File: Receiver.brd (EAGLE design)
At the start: 71.1 x 62.2 mm, 11 parts, among them IC1 25LC080P, J1 PIC_ICSP_6_PIN, U1 915MHz, U2 DS3234, X1 BU-SMA-V

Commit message: Updates
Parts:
- added BUTTON: TSW-106-02-S-S, con-samtec:TSW-106-02-S-S
- added C3, C4: (no value), resistor:C050-025X075
- added PWR: 22-27-2021-02, con-molex:6410-02
- added SJ1: SOLDERJUMPERNO, SparkFun-Retired:SJ_2S-NO
- moved RA8875 33.2 mm to (5.08, 41.9)
- moved X1 26.1 mm to (40.6, 5.08)
- moved IC1 18.2 mm to (20.3, 19.1), flipped to the bottom, turned to 270 degrees
- moved U1 13.3 mm to (40.6, 17.8)
- moved U2 13.3 mm to (40.6, 17.8)
- moved BT1 12.5 mm to (40.6, 43.2)
- moved Q1 2.54 mm to (5.08, 19.1)
- moved C1 2.29 mm to (1.91, 15.2), turned to 90 degrees
- moved C2 2.29 mm to (1.91, 22.9), turned to 270 degrees
- moved J1 1.27 mm to (14.0, 59.7)
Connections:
- net N$10 renamed MOSI1
- net N$11 renamed MOSI2
- net N$6 renamed SCK1
- net N$7 renamed MISO1
- net N$8 renamed SCK2
- net N$9 renamed MISO2
- new net N$10: BUTTON.4, U$1.19
- new net N$11: BUTTON.6, U$1.22
- new net N$17: RA8875.8, U$1.6
- new net N$18: RA8875.4, U$1.2
- new net N$19: RA8875.10, U$1.9
- new net N$20: RA8875.11, U$1.10
- new net N$21: U$1.30, U1.14
- new net N$22: J1.5, SJ1.1
- new net N$6: BUTTON.1, U$1.15
- new net N$7: BUTTON.2, U$1.16
- new net N$8: BUTTON.3, U$1.17
- new net N$9: BUTTON.5, U$1.20
- net +3V3: now also C3.1, C4.1, PWR.1, RA8875.1, SJ1.2; no longer J1.5
- net GND: now also C3.2, C4.2, PWR.2
- net N$12: now also U$1.29; no longer U$1.22
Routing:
- net +3V3: track 85.8 -> 141.4 mm, vias 1 -> 3
- net MISO1: track 0.00 -> 53.4 mm, vias 0 -> 1
- net SCK1: track 0.00 -> 48.0 mm
- net N$21: track 0.00 -> 31.8 mm, vias 0 -> 1
- net MISO2: track 75.8 -> 48.7 mm, vias 0 -> 1
- net MOSI1: track 0.00 -> 23.4 mm
- net N$11: track 0.00 -> 20.3 mm
- net GND: track 17.3 -> 0.00 mm
- net N$16: track 24.7 -> 14.3 mm
- net N$15: track 19.1 -> 10.2 mm, vias 1 -> 0
- net N$17: track 0.00 -> 8.15 mm
- net N$20: track 0.00 -> 8.15 mm
- net N$19: track 0.00 -> 8.15 mm
- net N$18: track 0.00 -> 8.15 mm
- net N$14: track 65.7 -> 58.2 mm
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- added copper zone on layer 1, net GND
- added copper zone on layer 16, net GND
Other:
- board size 71.1 x 62.2 mm -> 53.3 x 63.5 mm

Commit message: Ordered sender PCB
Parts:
- added IC2: 25LC080P, microchip:DIL8
- added J2: (no value), SparkFun-Connectors:1X01
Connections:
- net +3V3: now also IC1.3, IC1.7, IC2.3, IC2.7, IC2.8
- net GND: now also IC2.4, J2.1
- net MISO2: now also IC2.2
- net MOSI2: now also IC2.5
- net SCK2: now also IC2.6
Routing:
- net +3V3: track 141.4 -> 175.7 mm
- net MOSI2: track 33.3 -> 47.8 mm
- net MISO2: track 48.7 -> 62.1 mm
- net SCK2: track 54.1 -> 67.4 mm, vias 3 -> 5
- net MISO1: track 53.4 -> 54.9 mm

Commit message: Updated receiver PCB
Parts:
- removed J1: PIC_ICSP_6_PIN, SparkFun-Connectors:MOLEX-1X6
- added IC3: (no value), v-reg:78XXS
- added PWR1: 22-27-2021-02, con-molex:6410-02
- added R1, R2, R3, R4, R5, R6: (no value), resistor:M1206
- added X2: 53047-05, con-molex:53047-05
- moved J2 5.12 mm to (1.91, 6.99)
- moved C1 1.42 mm to (1.27, 16.5), turned to 270 degrees
- moved C2 1.42 mm to (1.27, 21.6), turned to 90 degrees
- moved BUTTON 0.63 mm to (10.2, 8.26)
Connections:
- new net N$23: IC2.1, U$1.25
- new net N$24: IC3.IN, PWR1.1
- net +3V3: now also IC3.OUT, R1.2, R2.2, R3.2, R4.2, R5.2, R6.2
- net GND: now also IC3.GND, PWR1.2, X2.3; no longer J1.4
- net N$1: now also X2.4; no longer J1.3
- net N$10: now also R4.1
- net N$11: now also R6.1
- net N$2: now also X2.5; no longer J1.2
- net N$22: now also X2.2; no longer J1.5
- net N$3: now also X2.1; no longer J1.6
- net N$6: now also R1.1
- net N$7: now also R2.1
- net N$8: now also R3.1
- net N$9: now also R5.1
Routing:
- net +3V3: track 175.7 -> 207.5 mm
- net N$24: track 0.00 -> 10.5 mm
- net N$3: track 20.6 -> 11.2 mm, vias 0 -> 1
- net N$23: track 0.00 -> 4.34 mm
- net N$2: track 20.6 -> 17.3 mm
- net N$22: track 3.99 -> 6.51 mm
- net N$11: track 20.3 -> 22.4 mm
- net N$9: track 3.96 -> 5.74 mm
- net N$8: track 3.44 -> 5.21 mm
- net N$7: track 3.44 -> 5.21 mm
- net N$6: track 3.44 -> 5.21 mm
- net N$10: track 3.96 -> 5.74 mm
- net N$1: track 15.5 -> 14.2 mm

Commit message: Receiver board r2
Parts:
- removed BT1: (no value), SparkFun-Batteries:BATTCON_20MM
- removed BUTTON: TSW-106-02-S-S, con-samtec:TSW-106-02-S-S
- removed IC1, IC2: 25LC080P, microchip:DIL8
- removed IC3: (no value), v-reg:78XXS
- removed PWR1: 22-27-2021-02, con-molex:6410-02
- removed Q1: (no value), crystal:HC49U-V
- removed R2, R3, R4, R5, R6: (no value), resistor:M1206
- removed SJ1: SOLDERJUMPERNO, SparkFun-Retired:SJ_2S-NO
- removed U$1: PIC18F47K40, microchip:DIL40
- added C5, C6: (no value), resistor:C1206
- added C7: 0.1uF, resistor:C1206
- added I2C-DBG: (no value), SparkFun-Connectors:1X03
- added J1: SD_CARD_SOCKET, SparkFun-Connectors:SD
- added RA8875-DBG: (no value), SparkFun-Connectors:1X09
- added SPI2-DBG: (no value), SparkFun-Connectors:1X08
- added TP3V3, TPCLKOUT, TPSQW, TPVBUS: TPB2,54, testpad:B2,54
- added U$3: (no value), adafruit:CR1220-SMD
- added U4: FT232RL, SparkFun-IC-Comms:SSOP28DB
- added U5: DS1374C, FRC696:SO-16DW
- added U6: +12v, SparkFun-IC-Power:TO-252
- added UARTDBG: 53047-03, con-molex:53047-03
- C1: value (none) -> 0.1uF
- C2: value (none) -> 1uF
- C3: value (none) -> 0.1uF; device resistor:C050-025X075 -> resistor:C1206
- C4: value (none) -> 1uF; device resistor:C050-025X075 -> resistor:C1206
- J2: device SparkFun-Connectors:1X01 -> SparkFun-Connectors:USB-B-MICRO-SMD
- PWR: value 22-27-2021-02 -> 53261-02; device con-molex:6410-02 -> con-molex:53261-02
- R1: value (none) -> 10k; device resistor:M1206 -> resistor:R1206
- RA8875: value C-GRID-11-70543 -> C-GRID-10-70543; device con-molex:70543-11 -> con-molex:70543-10
- U1: value 915MHz -> PIC18F47Q84; device SparkFun-RF:RFM69HCW-XXXS2 -> FRC696:DIL40
- U2: value DS3234 -> 915MHz; device SparkFun-Clocks:SO20-0.3 -> SparkFun-RF:RFM69HCW-XXXS2
- X2: value 53047-05 -> PIC-PROG047; device con-molex:53047-05 -> FRC696:53047-05
- moved J2 88.5 mm to (73.0, 59.7), turned to 180 degrees
- moved C1 82.2 mm to (59.1, 74.9), flipped to the top
- moved C2 75.9 mm to (55.2, 74.9), flipped to the top, turned to 270 degrees
- moved R1 60.3 mm to (18.4, 73.7), flipped to the top, turned to 90 degrees
- moved X1 47.7 mm to (63.5, 47.0)
- moved PWR 41.3 mm to (71.8, 69.8), turned to 270 degrees
- moved RA8875 36.3 mm to (24.8, 11.4), turned to 0 degrees
- moved U1 30.4 mm to (26.0, 44.5), turned to 270 degrees
- moved X2 20.8 mm to (26.0, 73.7)
- moved C3 19.9 mm to (40.0, 73.7), turned to 270 degrees
- moved U2 17.6 mm to (56.5, 25.4), flipped to the top
- moved C4 13.1 mm to (36.2, 73.7), turned to 270 degrees
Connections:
- removed net N$14: BT1.1, U2.16
- removed net N$15: U$1.24, U1.5
- removed net N$16: U$1.21, U2.1
- removed net N$17: RA8875.8, U$1.6
- removed net N$18: RA8875.4, U$1.2
- removed net N$19: RA8875.10, U$1.9
- removed net N$20: RA8875.11, U$1.10
- removed net N$21: U$1.30, U1.14
- removed net N$22: SJ1.1, X2.2
- removed net N$23: IC2.1, U$1.25
- removed net N$24: IC3.IN, PWR1.1
- new net CLK_RST: U5.14
- new net RA8875-CS: RA8875-DBG.6, RA8875.7, U1.30
- new net RA8875-INT: RA8875-DBG.9, RA8875.10, U1.23
- new net RA8875-LITE: RA8875-DBG.2, RA8875.3, U1.19
- new net RA8875-RST: RA8875-DBG.7, RA8875.8, U1.29
- new net RA8875-WAIT: RA8875-DBG.8, RA8875.9, U1.28
- new net RF-CS: SPI2-DBG.5, U1.24, U2.5
- new net RF-DIO0: SPI2-DBG.7, U1.26, U2.14
- new net RF-RST: SPI2-DBG.6, U1.25, U2.6
- new net SCL: I2C-DBG.2, U1.38, U5.1
- new net SD-CS: J1.1, SPI2-DBG.8, U1.27
- new net SDA: I2C-DBG.3, U1.37, U5.16
- new net UARTRX: U1.35, U4.1, UARTDBG.3
- new net UARTTX: U1.34, U4.5, UARTDBG.2
- net +3V3: now also C5.1, C6.1, J1.4, TP3V3.TP, U1.11, U1.32, U2.13, U4.20, U4.4, U5.4, U6.2, X2.2; no longer IC1.3, IC1.7, IC1.8, IC2.3, IC2.7, IC2.8, IC3.OUT, PWR.1, R2.2, R3.2, R4.2, R5.2, R6.2, SJ1.2, U$1.11, U$1.32, U1.13, U2.4
- net GND: now also C1.2, C2.2, C5.2, C6.2, C7.2, I2C-DBG.1, J1.3, J1.6, J1.SH@1, J1.SH@2, J2.GND, RA8875-DBG.1, SPI2-DBG.1, U$3.-, U1.12, U1.31, U2.1, U4.18, U4.21, U4.25, U4.26, U4.7, U5.15, U6.3, UARTDBG.1; no longer BT1.2, C1.1, C2.1, IC1.4, IC2.4, IC3.GND, J2.1, PWR1.2, U$1.12, U$1.31, U1.1, U1.10, U1.8, U2.11, U2.12, U2.13, U2.14, U2.15, U2.2, U2.7, U2.9
- net MISO1: now also RA8875-DBG.4, RA8875.5, U1.17; no longer RA8875.6, U$1.23
- net MISO2: now also J1.7, SPI2-DBG.2, U1.21, U2.2; no longer IC1.2, IC2.2, U$1.35, U1.2, U2.19
- net MOSI1: now also RA8875-DBG.5, RA8875.6, U1.16; no longer RA8875.7, U$1.36
- net MOSI2: now also J1.2, SPI2-DBG.3, U1.22, U2.3; no longer IC1.5, IC2.5, U$1.27, U1.3, U2.17
- net N$1: now also U1.39, X2.5; no longer U$1.40, X2.4
- net N$10: now also U$3.+$1, U$3.+$2, U5.13; no longer BUTTON.4, R4.1, U$1.19
- net N$11: now also TPSQW.TP, U5.3; no longer BUTTON.6, R6.1, U$1.22
- net N$12: now also TPCLKOUT.TP, U1.14; no longer IC1.1, U$1.29
- net N$13: now also U2.9; no longer U1.9
- net N$2: now also U1.40, X2.4; no longer U$1.39, X2.5
- net N$3: now also R1.1, U1.1; no longer U$1.1
- net N$4: now also C1.1, C2.1, PWR.1, U6.1; no longer C1.2, Q1.2, U$1.14
- net N$5: now also J2.VBUS, TPVBUS.TP; no longer C2.2, Q1.1, U$1.13
- net N$6: now also C7.1, U4.17; no longer BUTTON.1, R1.1, U$1.15
- net N$7: now also J2.D-, U4.16; no longer BUTTON.2, R2.1, U$1.16
- net N$8: now also J2.D+, U4.15; no longer BUTTON.3, R3.1, U$1.17
- net N$9: now also U1.15; no longer BUTTON.5, R5.1, U$1.20
- net SCK1: now also RA8875-DBG.3, RA8875.4, U1.18; no longer RA8875.5, U$1.18
- net SCK2: now also J1.5, SPI2-DBG.4, U1.20, U2.4; no longer IC1.6, IC2.6, U$1.34, U1.4, U2.18, U2.20
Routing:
- net N$14: track 58.2 -> 0.00 mm, vias 1 -> 0
- net RA8875-CS: track 0.00 -> 45.3 mm
- net RA8875-RST: track 0.00 -> 42.7 mm
- net RA8875-WAIT: track 0.00 -> 40.2 mm
- net SD-CS: track 0.00 -> 39.6 mm
- net SCL: track 0.00 -> 37.3 mm
- net N$10: track 5.74 -> 42.3 mm
- net RF-RST: track 0.00 -> 34.5 mm
- net +3V3: track 207.5 -> 240.9 mm, vias 3 -> 2
- net N$21: track 31.8 -> 0.00 mm, vias 1 -> 0
- net RF-CS: track 0.00 -> 31.1 mm
- net UARTRX: track 0.00 -> 28.5 mm
- net SDA: track 0.00 -> 27.6 mm
- net RA8875-INT: track 0.00 -> 26.8 mm
- net UARTTX: track 0.00 -> 26.1 mm
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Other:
- board size 53.3 x 63.5 mm -> 74.9 x 81.3 mm
- board text added: "TEMP MONITOR R2"

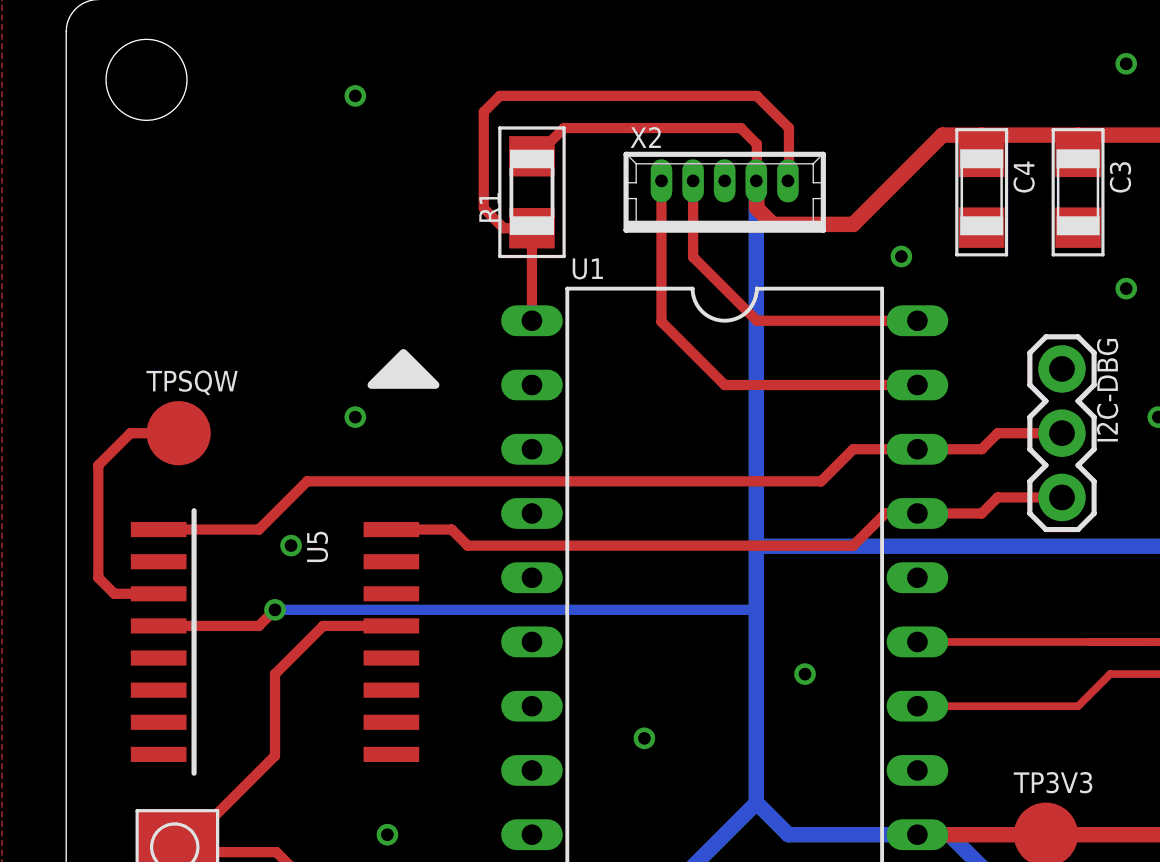
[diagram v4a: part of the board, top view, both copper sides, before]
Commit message: Adding button inputs
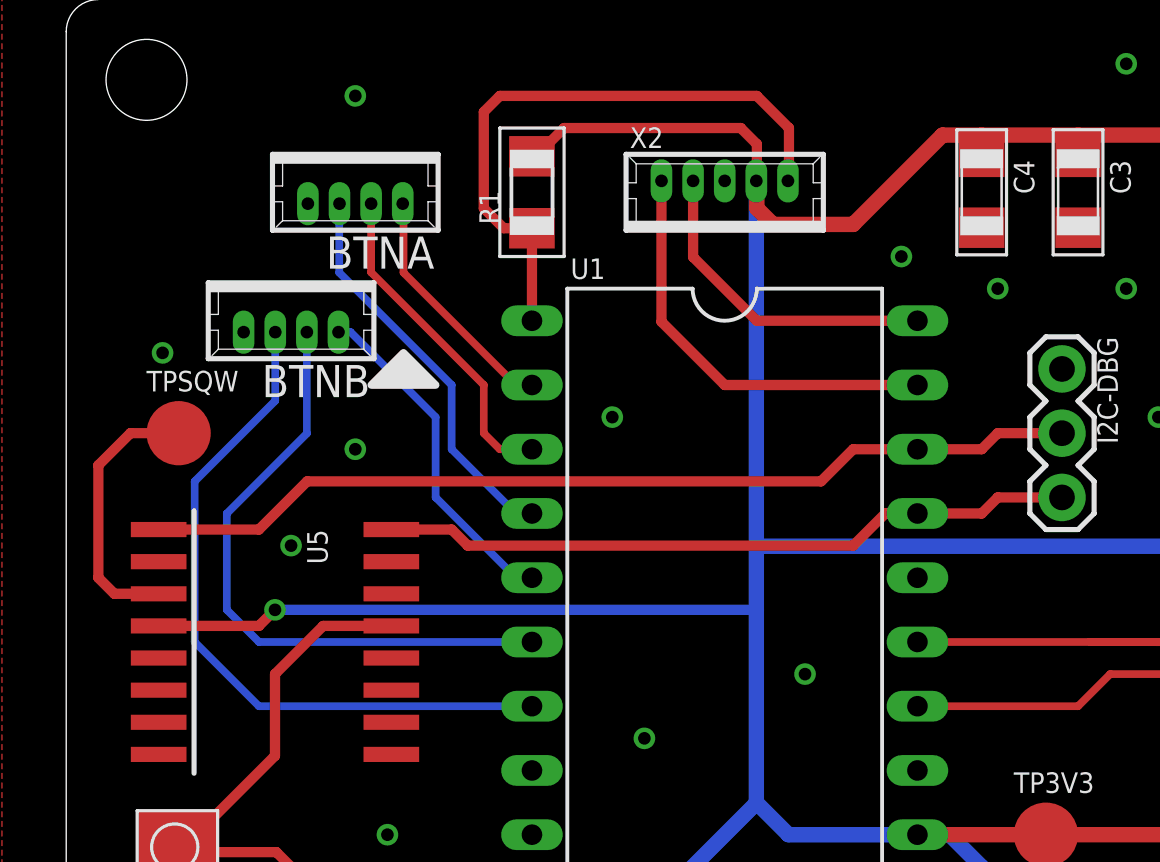
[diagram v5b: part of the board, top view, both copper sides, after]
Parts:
- added BTNA, BTNB: 53047-04, con-molex:53047-04
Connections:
- new net BTN1: BTNA.2, U1.4
- new net BTN2: BTNA.3, U1.3
- new net BTN3: BTNA.4, U1.2
- new net BTN4: BTNB.2, U1.7
- new net BTN5: BTNB.3, U1.6
- new net BTN6: BTNB.4, U1.5
- net GND: now also BTNA.1, BTNB.1
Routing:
- net BTN4: track 0.00 -> 28.0 mm
- net BTN5: track 0.00 -> 24.9 mm
- net BTN1: track 0.00 -> 15.8 mm
- net BTN6: track 0.00 -> 13.5 mm
- net BTN2: track 0.00 -> 13.1 mm
- net BTN3: track 0.00 -> 9.66 mm
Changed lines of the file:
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@@
 <attribute name="VALUE" x="37.338" y="67.945" size="0.6096" layer="27" font="vector" ratio="20" rot="R270"/>
+</element>
+<element name="BTNB" library="con-molex" package="53047-04" value="53047-04" x="8.89" y="68.58" smashed="yes" rot="R180">
+<attribute name="MF" value="WALDOM/MOLEX" x="8.89" y="68.58" size="0.8128" layer="27" font="fixed" rot="R180" display="off"/>
+<attribute name="OC_NEWARK" value="38C9900" x="8.89" y="68.58" size="0.8128" layer="27" font="fixed" rot="R180" display="off"/>
+<attribute name="OC_FARNELL" value="9733060" x="8.89" y="68.58" size="0.8128" layer="27" font="fixed" rot="R180" display="off"/>
+<attribute name="MPN" value="53047-0410" x="8.89" y="68.58" size="0.8128" layer="27" font="fixed" rot="R180" display="off"/>
+<attribute name="NAME" x="12.015" y="66.83" size="1.27" layer="25" font="fixed" rot="R180"/>
+</element>
+<element name="BTNA" library="con-molex" package="53047-04" value="53047-04" x="11.43" y="73.66" smashed="yes" rot="R180">
+<attribute name="MF" value="WALDOM/MOLEX" x="11.43" y="73.66" size="0.8128" layer="27" font="fixed" rot="R180" display="off"/>
+<attribute name="OC_NEWARK" value="38C9900" x="11.43" y="73.66" size="0.8128" layer="27" font="fixed" rot="R180" display="off"/>
+<attribute name="OC_FARNELL" value="9733060" x="11.43" y="73.66" size="0.8128" layer="27" font="fixed" rot="R180" display="off"/>
+<attribute name="MPN" value="53047-0410" x="11.43" y="73.66" size="0.8128" layer="27" font="fixed" rot="R180" display="off"/>
+<attribute name="NAME" x="14.555" y="71.91" size="1.27" layer="25" font="fixed" rot="R180"/>
 </element>
 </elements>
@@
 <contactref element="X1" pad="4"/>
 <contactref element="X1" pad="5"/>
-<contactref element="U6" pad="3"/>
 <contactref element="U6" pad="3"/>
 <contactref element="PWR" pad="2"/>
@@
 <via x="3.81" y="35.56" extent="1-16" drill="0.5"/>
 <via x="8.89" y="59.69" extent="1-16" drill="0.5"/>
-<via x="11.43" y="64.77" extent="1-16" drill="0.5"/>
 <via x="11.43" y="77.47" extent="1-16" drill="0.5"/>
 <via x="41.91" y="78.74" extent="1-16" drill="0.5"/>
@@
 <via x="64.77" y="41.91" extent="1-16" drill="0.5"/>
 <via x="33.02" y="71.12" extent="1-16" drill="0.5"/>
+<contactref element="BTNA" pad="1"/>
+<contactref element="BTNB" pad="1"/>
+<via x="11.43" y="63.5" extent="1-16" drill="0.5"/>
+<via x="3.81" y="67.31" extent="1-16" drill="0.5"/>
+<via x="21.59" y="64.77" extent="1-16" drill="0.5"/>
+<via x="36.83" y="69.85" extent="1-16" drill="0.5"/>
 </signal>
 <signal name="MISO2">
@@
 <wire x1="4.445" y1="64.135" x2="2.54" y2="64.135" width="0.4064" layer="1"/>
 </signal>
+<signal name="BTN1">
+<contactref element="BTNA" pad="2"/>
+<contactref element="U1" pad="4"/>
+<wire x1="18.415" y1="60.96" x2="17.78" y2="60.96" width="0.3048" layer="16"/>
+<wire x1="17.78" y1="60.96" x2="15.24" y2="63.5" width="0.3048" layer="16"/>
+<wire x1="15.24" y1="63.5" x2="15.24" y2="66.04" width="0.3048" layer="16"/>
+<wire x1="15.24" y1="66.04" x2="10.795" y2="70.485" width="0.3048" layer="16"/>
+<wire x1="10.795" y1="70.485" x2="10.795" y2="73.2" width="0.3048" layer="16"/>
+<wire x1="10.795" y1="73.2" x2="10.805" y2="73.21" width="0.3048" layer="16"/>
+</signal>
+<signal name="BTN2">
+<contactref element="BTNA" pad="3"/>
+<contactref element="U1" pad="3"/>
+<wire x1="18.415" y1="63.5" x2="17.145" y2="63.5" width="0.3048" layer="1"/>
+<wire x1="17.145" y1="63.5" x2="16.51" y2="64.135" width="0.3048" layer="1"/>
+<wire x1="16.51" y1="64.135" x2="16.51" y2="66.04" width="0.3048" layer="1"/>
+<wire x1="16.51" y1="66.04" x2="12.055" y2="70.495" width="0.3048" layer="1"/>
+<wire x1="12.055" y1="73.21" x2="12.055" y2="70.495" width="0.3048" layer="1"/>
+</signal>
+<signal name="BTN3">
+<contactref element="BTNA" pad="4"/>
+<contactref element="U1" pad="2"/>
+<wire x1="18.415" y1="66.04" x2="17.78" y2="66.04" width="0.3048" layer="1"/>
+<wire x1="17.78" y1="66.04" x2="13.335" y2="70.485" width="0.3048" layer="1"/>
+<wire x1="13.335" y1="70.485" x2="13.335" y2="73.18" width="0.3048" layer="1"/>
+<wire x1="13.335" y1="73.18" x2="13.305" y2="73.21" width="0.3048" layer="1"/>
+</signal>
+<signal name="BTN6">
+<contactref element="BTNB" pad="4"/>
+<contactref element="U1" pad="5"/>
+<wire x1="18.415" y1="58.42" x2="17.78" y2="58.42" width="0.3048" layer="16"/>
+<wire x1="17.78" y1="58.42" x2="14.605" y2="61.595" width="0.3048" layer="16"/>
+<wire x1="14.605" y1="61.595" x2="14.605" y2="64.77" width="0.3048" layer="16"/>
+<wire x1="14.605" y1="64.77" x2="11.245" y2="68.13" width="0.3048" layer="16"/>
+<wire x1="10.765" y1="68.13" x2="11.245" y2="68.13" width="0.3048" layer="16"/>
+</signal>
+<signal name="BTN5">
+<contactref element="BTNB" pad="3"/>
+<contactref element="U1" pad="6"/>
+<wire x1="18.415" y1="55.88" x2="7.62" y2="55.88" width="0.3048" layer="16"/>
+<wire x1="7.62" y1="55.88" x2="6.35" y2="57.15" width="0.3048" layer="16"/>
+<wire x1="6.35" y1="57.15" x2="6.35" y2="60.96" width="0.3048" layer="16"/>
+<wire x1="6.35" y1="60.96" x2="9.515" y2="64.125" width="0.3048" layer="16"/>
+<wire x1="9.515" y1="68.13" x2="9.515" y2="64.125" width="0.3048" layer="16"/>
+</signal>
+<signal name="BTN4">
+<contactref element="BTNB" pad="2"/>
+<contactref element="U1" pad="7"/>
+<wire x1="18.415" y1="53.34" x2="7.62" y2="53.34" width="0.3048" layer="16"/>
+<wire x1="7.62" y1="53.34" x2="5.08" y2="55.88" width="0.3048" layer="16"/>
+<wire x1="5.08" y1="55.88" x2="5.08" y2="62.23" width="0.3048" layer="16"/>
+<wire x1="5.08" y1="62.23" x2="8.265" y2="65.415" width="0.3048" layer="16"/>
+<wire x1="8.265" y1="68.13" x2="8.265" y2="65.415" width="0.3048" layer="16"/>
+</signal>
 </signals>

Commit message: PCB updates
- Connected NC pins of DS1374 to GND
- Connected CLK_RST to PIC
- Moved I2C to default pins on PIC
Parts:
- C5: value (none) -> 10uF
- C6: value (none) -> 0.1uF
- moved I2C-DBG 52.3 mm to (14.0, 21.0), turned to 90 degrees
- moved TPSQW 50.8 mm to (4.45, 13.3)
- moved U5 33.7 mm to (6.35, 22.2), turned to 0 degrees
- moved BTNB 13.6 mm to (11.4, 55.2), turned to 270 degrees
- moved BTNA 10.8 mm to (11.4, 62.9), turned to 270 degrees
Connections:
- net RA8875-CS renamed RA8875_CS
- net RA8875-RST renamed RA8875_RST
- net RA8875-WAIT renamed RA8875_WAIT
- net SD-CS renamed SD_CS
- removed net N$9: U1.15
- removed net RA8875-INT: RA8875-DBG.9, RA8875.10, U1.23
- removed net RF-DIO0: SPI2-DBG.7, U1.26, U2.14
- new net CLK_INT: U1.34, U5.2
- new net RA8875_INT: RA8875-DBG.9, RA8875.10, U1.33
- new net RF_DIO0: SPI2-DBG.7, U1.35, U2.14
- new net SD_CD: J1.CD, U1.26
- net CLK_RST: now also U1.13
- net GND: now also U5.10, U5.11, U5.12, U5.5, U5.6, U5.7, U5.8, U5.9
- net MISO1: now also U1.16; no longer U1.17
- net MOSI1: now also U1.15; no longer U1.16
- net SCK1: now also U1.17; no longer U1.18
- net SCL: now also U1.18; no longer U1.38
- net SDA: now also U1.23; no longer U1.37
- net UARTRX: now also U1.37; no longer U1.35
- net UARTTX: now also U1.36; no longer U1.34
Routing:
- net CLK_INT: track 0.00 -> 59.1 mm, vias 0 -> 2
- net RF_DIO0: track 0.00 -> 54.5 mm, vias 0 -> 1
- net RA8875_INT: track 0.00 -> 52.2 mm, vias 0 -> 1
- net SD_CD: track 0.00 -> 37.7 mm, vias 0 -> 3
- net CLK_RST: track 0.00 -> 27.5 mm
- net RA8875-INT: track 26.8 -> 0.00 mm
- net RF-DIO0: track 22.9 -> 0.00 mm
- net BTN4: track 28.0 -> 7.07 mm
- net BTN5: track 24.9 -> 6.54 mm
- net SCL: track 37.3 -> 21.3 mm
- net +3V3: track 240.9 -> 228.2 mm, vias 2 -> 1
- net N$10: track 42.3 -> 30.1 mm
- net BTN1: track 15.8 -> 7.07 mm
- net SDA: track 27.6 -> 35.7 mm
- net BTN2: track 13.1 -> 6.54 mm
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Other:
- board text added: "TEMP MONITOR R3"
- board text removed: "TEMP MONITOR R2"
